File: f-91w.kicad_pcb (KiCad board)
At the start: 4 copper layers, 24.4 x 24.4 mm, 93 parts, among them P1 CONN_01X01, P10 CONN_01X01, P11 CONN_01X01, P13 CONN_01X01, P14 CONN_01X01, P2 CONN_01X01, P3 CONN_01X01, P5 CONN_01X01, P6 CONN_01X01, P7 CONN_01X01, P8 CONN_01X01, P9 CONN_01X01, Q1 BC846, U1 CY8C4248LQI-BL483, U2 LCD-F-91W, U3 BME680, Y1 32.768KHz, Y2 24MHz

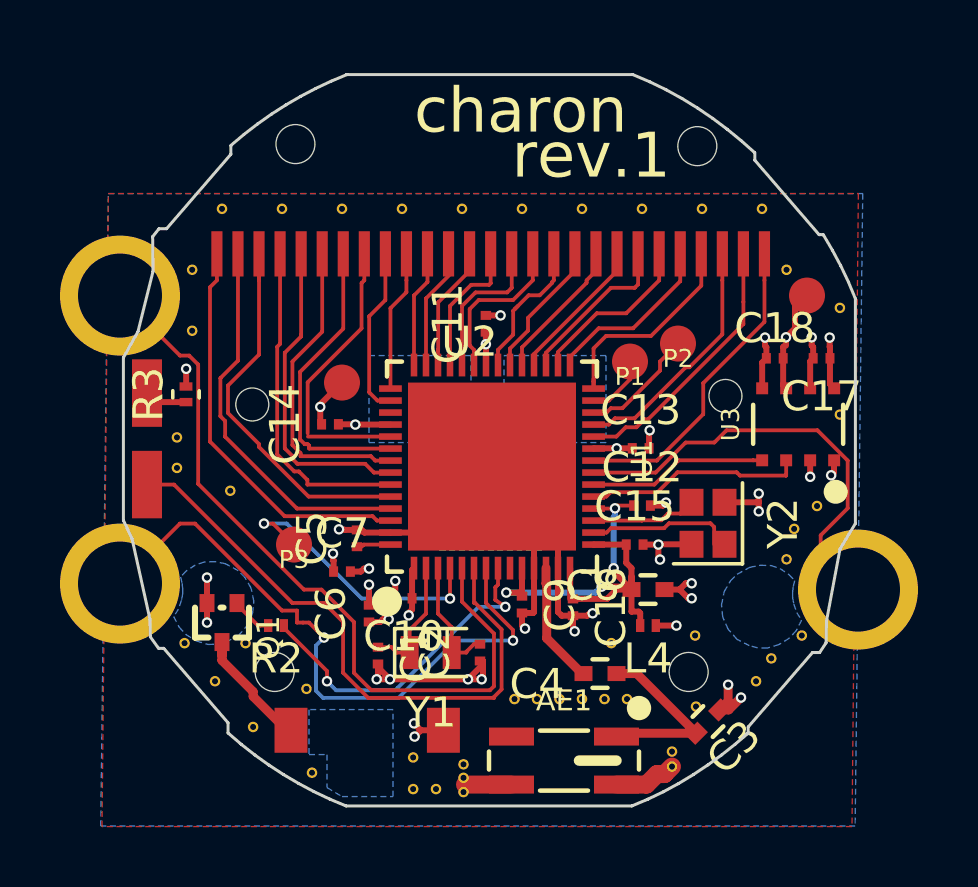
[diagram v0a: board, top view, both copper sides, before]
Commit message: Tidy silkscreen and gloss some tracks for demo
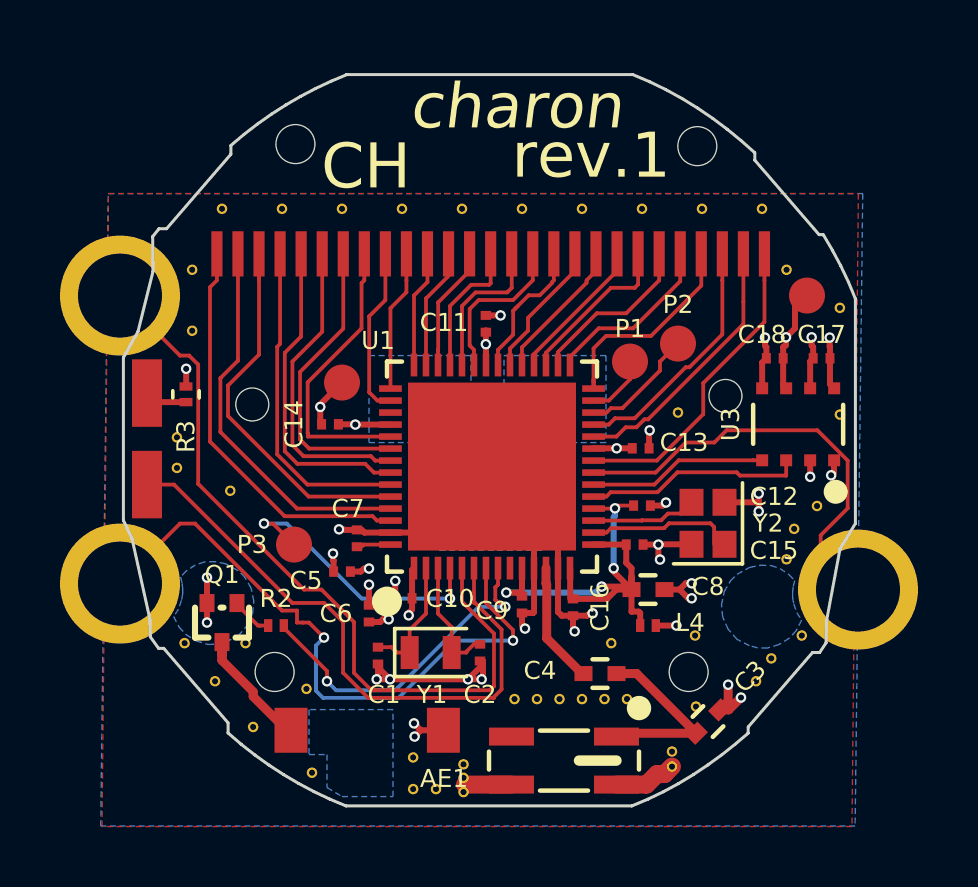
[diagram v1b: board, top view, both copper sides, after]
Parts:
- added REF**: STITCHING_VIA_0.2mm, f-91w:STITCHING_VIA_0.2mm, F.Cu at (64.2, 96.2)
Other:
- board text added: "CH"

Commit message: Make antenna trace 50R coplanar to match eurocircuits stackup
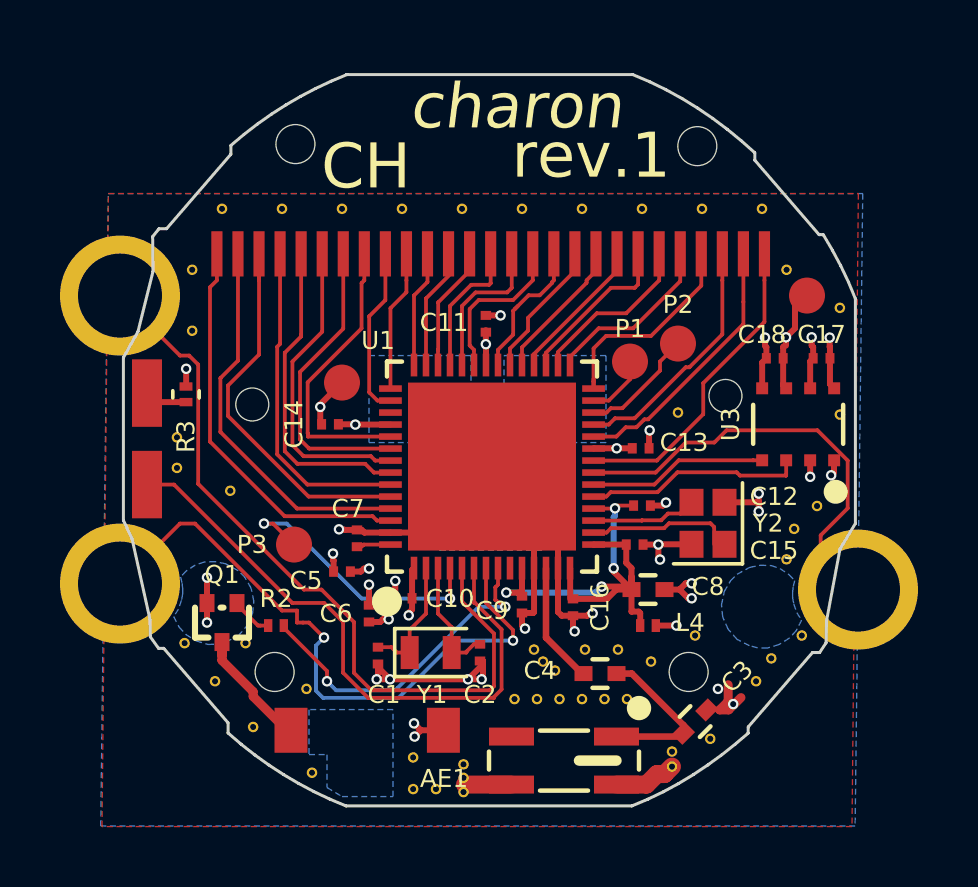
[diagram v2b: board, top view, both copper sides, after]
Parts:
- removed the REF** at (64.8, 106.0)
- added REF**: STITCHING_VIA_0.2mm, f-91w:STITCHING_VIA_0.2mm, F.Cu at (65.3, 107.1)
- added REF**: STITCHING_VIA_0.2mm, f-91w:STITCHING_VIA_0.2mm, F.Cu at (59.7, 104.5)
- added REF**: STITCHING_VIA_0.2mm, f-91w:STITCHING_VIA_0.2mm, F.Cu at (63.3, 104.5)
- added REF**: STITCHING_VIA_0.2mm, f-91w:STITCHING_VIA_0.2mm, F.Cu at (61.1, 104.1)
- added REF**: STITCHING_VIA_0.2mm, f-91w:STITCHING_VIA_0.2mm, F.Cu at (59.4, 104.1)
- added REF**: STITCHING_VIA_0.2mm, f-91w:STITCHING_VIA_0.2mm, F.Cu at (60.1, 104.8)
- moved C3 0.43 mm to (64.8, 106.5)
- moved REF** 0.31 mm to (62.2, 104.1)
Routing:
- net Net-(AE1-Pad1): track 6.19 -> 5.49 mm
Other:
- net class ANT added: clearance 0.18, trace_width 0.22, via_dia 0.35, via_drill 0.2
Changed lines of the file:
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@@
     (links 153)
     (no_connects 0)
-    (area 45.663181 84.883147 70.163247 109.362848)
+    (area 39.501571 84.8 74.608715 110.532)
     (thickness 0.6)
     (drawings 509)
-    (tracks 518)
+    (tracks 517)
     (zones 0)
-    (modules 94)
+    (modules 99)
     (nets 51)
   )
@@
   (layers
     (0 F.Cu signal)
-    (1 In1.Cu power hide)
-    (2 In2.Cu signal hide)
+    (1 In1.Cu power)
+    (2 In2.Cu signal)
     (31 B.Cu signal)
     (32 B.Adhes user hide)
@@
     (39 F.Mask user)
     (40 Dwgs.User user hide)
-    (41 Cmts.User user)
+    (41 Cmts.User user hide)
     (42 Eco1.User user hide)
     (43 Eco2.User user hide)
@@
     (visible_elements 7FFEFF7F)
     (pcbplotparams
-      (layerselection 0x010f0_80000001)
+      (layerselection 0x010f0_80000007)
       (usegerberextensions true)
       (excludeedgelayer true)
@@
     (add_net /SWCLK)
     (add_net /SWDIO)
-    (add_net "Net-(AE1-Pad1)")
     (add_net "Net-(C1-Pad1)")
     (add_net "Net-(C2-Pad1)")
-    (add_net "Net-(C4-Pad1)")
     (add_net "Net-(C5-Pad2)")
     (add_net "Net-(P10-Pad1)")
@@
     (add_net "Net-(U1-Pad16)")
     (add_net "Net-(U1-Pad17)")
+  )
+  (net_class ANT ""
+    (clearance 0.18)
+    (trace_width 0.22)
+    (via_dia 0.35)
+    (via_drill 0.2)
+    (uvia_dia 0.3)
+    (uvia_drill 0.1)
+    (add_net "Net-(AE1-Pad1)")
+    (add_net "Net-(C4-Pad1)")
   )
   (net_class PWR ""
@@
   )
   (module f-91w:STITCHING_VIA_0.2mm (layer F.Cu)
+    (at 65.275 107.075)
+    (fp_text reference REF** (at 0 1) (layer F.SilkS) hide
+      (effects (font (size 0.6 0.6) (thickness 0.15)))
+    )
+    (fp_text value STITCHING_VIA_0.2mm (at 0 -0.5) (layer F.Fab) hide
+      (effects (font (size 0.6 0.6) (thickness 0.15)))
+    )
+    (pad 1 thru_hole circle (at 0 0) (size 0.35 0.35) (drill 0.2) (layers *.Cu)
+      (net 2 GND) (zone_connect 2))
+  )
+  (module f-91w:STITCHING_VIA_0.2mm (layer F.Cu)
+    (at 59.7 104.5)
+    (fp_text reference REF** (at 0 1) (layer F.SilkS) hide
+      (effects (font (size 0.6 0.6) (thickness 0.15)))
+    )
+    (fp_text value STITCHING_VIA_0.2mm (at 0 -0.5) (layer F.Fab) hide
+      (effects (font (size 0.6 0.6) (thickness 0.15)))
+    )
+    (pad 1 thru_hole circle (at 0 0) (size 0.35 0.35) (drill 0.2) (layers *.Cu)
+      (net 2 GND) (zone_connect 2))
+  )
+  (module f-91w:STITCHING_VIA_0.2mm (layer F.Cu)
+    (at 63.3 104.5)
+    (fp_text reference REF** (at 0 1) (layer F.SilkS) hide
+      (effects (font (size 0.6 0.6) (thickness 0.15)))
+    )
+    (fp_text value STITCHING_VIA_0.2mm (at 0 -0.5) (layer F.Fab) hide
+      (effects (font (size 0.6 0.6) (thickness 0.15)))
+    )
+    (pad 1 thru_hole circle (at 0 0) (size 0.35 0.35) (drill 0.2) (layers *.Cu)
+      (net 2 GND) (zone_connect 2))
+  )
+  (module f-91w:STITCHING_VIA_0.2mm (layer F.Cu)
+    (at 61.1 104.1)
+    (fp_text reference REF** (at 0 1) (layer F.SilkS) hide
+      (effects (font (size 0.6 0.6) (thickness 0.15)))
+    )
+    (fp_text value STITCHING_VIA_0.2mm (at 0 -0.5) (layer F.Fab) hide
+      (effects (font (size 0.6 0.6) (thickness 0.15)))
+    )
+    (pad 1 thru_hole circle (at 0 0) (size 0.35 0.35) (drill 0.2) (layers *.Cu)
+      (net 2 GND) (zone_connect 2))
+  )
+  (module f-91w:STITCHING_VIA_0.2mm (layer F.Cu)
+    (at 59.4 104.1)
+    (fp_text reference REF** (at 0 1) (layer F.SilkS) hide
+      (effects (font (size 0.6 0.6) (thickness 0.15)))
+    )
+    (fp_text value STITCHING_VIA_0.2mm (at 0 -0.5) (layer F.Fab) hide
+      (effects (font (size 0.6 0.6) (thickness 0.15)))
+    )
+    (pad 1 thru_hole circle (at 0 0) (size 0.35 0.35) (drill 0.2) (layers *.Cu)
+      (net 2 GND) (zone_connect 2))
+  )
+  (module f-91w:STITCHING_VIA_0.2mm (layer F.Cu)
+    (at 60.1 104.8)
+    (fp_text reference REF** (at 0 1) (layer F.SilkS) hide
+      (effects (font (size 0.6 0.6) (thickness 0.15)))
+    )
+    (fp_text value STITCHING_VIA_0.2mm (at 0 -0.5) (layer F.Fab) hide
+      (effects (font (size 0.6 0.6) (thickness 0.15)))
+    )
+    (pad 1 thru_hole circle (at 0 0) (size 0.35 0.35) (drill 0.2) (layers *.Cu)
+      (net 2 GND) (zone_connect 2))
+  )
+  (module f-91w:STITCHING_VIA_0.2mm (layer F.Cu)
     (at 64.2 96.2)
     (fp_text reference REF** (at 0 1) (layer F.SilkS) hide
@@
   )
   (module f-91w:STITCHING_VIA_0.2mm (layer F.Cu)
-    (at 64.8 106)
-    (fp_text reference REF** (at 0 1) (layer F.SilkS) hide
-      (effects (font (size 0.6 0.6) (thickness 0.15)))
-    )
-    (fp_text value STITCHING_VIA_0.2mm (at 0 -0.5) (layer F.Fab) hide
-      (effects (font (size 0.6 0.6) (thickness 0.15)))
-    )
-    (pad 1 thru_hole circle (at 0 0) (size 0.35 0.35) (drill 0.2) (layers *.Cu)
-      (net 2 GND) (zone_connect 2))
-  )
-  (module f-91w:STITCHING_VIA_0.2mm (layer F.Cu)
     (at 62.5 105.75)
     (fp_text reference REF** (at 0 1) (layer F.SilkS) hide
@@
   )
   (module f-91w:STITCHING_VIA_0.2mm (layer F.Cu)
-    (at 61.976 103.886)
+    (at 62.2 104.1)
     (fp_text reference REF** (at 0 1) (layer F.SilkS) hide
       (effects (font (size 0.6 0.6) (thickness 0.15)))
@@
   )
   (module Capacitors_SMD:C_0402 (layer F.Cu)
-    (at 65.2 106.5 45)
+    (at 64.77 106.5 45)
     (descr "Capacitor SMD 0402, reflow soldering, AVX (see smccp.pdf)")
     (tags "capacitor 0402")
@@
   (segment (start 65.588909 106.111091) (end 65.888909 106.111091) (width 0.3) (layer F.Cu) (net 2))
   (segment (start 65.888909 106.111091) (end 66.3 105.7) (width 0.3) (layer F.Cu) (net 2))
-  (via (at 66.3 105.7) (size 0.35) (drill 0.2) (layers F.Cu B.Cu) (net 2))
-  (via (at 65.871751 105.271751) (size 0.35) (drill 0.2) (layers F.Cu B.Cu) (net 2))
+  (via (at 66.04 105.918) (size 0.35) (drill 0.2) (layers F.Cu B.Cu) (net 2))
+  (via (at 65.532 105.41) (size 0.35) (drill 0.2) (layers F.Cu B.Cu) (net 2))
   (segment (start 65.588909 106.111091) (end 65.871751 105.828249) (width 0.3) (layer F.Cu) (net 2))
   (segment (start 65.871751 105.828249) (end 65.871751 105.271751) (width 0.3) (layer F.Cu) (net 2))
@@
   (segment (start 56.2 101.385) (end 56.2 102.9) (width 0.127) (layer F.Cu) (net 40))
   (segment (start 56.2 102.9) (end 56.6555 103.3555) (width 0.127) (layer F.Cu) (net 40))
-  (segment (start 64.811091 106.888909) (end 62.261091 106.888909) (width 0.3) (layer F.Cu) (net 41))
-  (segment (start 62.261091 106.888909) (end 62.15 107) (width 0.3) (layer F.Cu) (net 41))
-  (segment (start 62.15 104.9) (end 62.822182 104.9) (width 0.3) (layer F.Cu) (net 41))
-  (segment (start 62.822182 104.9) (end 64.811091 106.888909) (width 0.3) (layer F.Cu) (net 41))
-  (segment (start 59.8 101.385) (end 59.8 101.9) (width 0.3) (layer F.Cu) (net 42))
-  (segment (start 59.8 101.9) (end 59.82299 101.92299) (width 0.3) (layer F.Cu) (net 42))
-  (segment (start 59.82299 101.92299) (end 59.82299 103.72299) (width 0.3) (layer F.Cu) (net 42))
-  (segment (start 59.82299 103.72299) (end 61 104.9) (width 0.3) (layer F.Cu) (net 42))
-  (segment (start 61 104.9) (end 61.05 104.9) (width 0.3) (layer F.Cu) (net 42))
+  (segment (start 62.15 107) (end 64.27 107) (width 0.22) (layer F.Cu) (net 41))
+  (segment (start 64.27 107) (end 64.381091 106.888909) (width 0.21) (layer F.Cu) (net 41))
+  (segment (start 62.15 104.9) (end 62.66 104.9) (width 0.22) (layer F.Cu) (net 41))
+  (segment (start 62.66 104.9) (end 64.381091 106.621091) (width 0.22) (layer F.Cu) (net 41))
+  (segment (start 64.381091 106.621091) (end 64.381091 106.888909) (width 0.22) (layer F.Cu) (net 41))
+  (segment (start 59.8 101.385) (end 59.8 103.7) (width 0.22) (layer F.Cu) (net 42))
+  (segment (start 59.8 103.7) (end 61 104.9) (width 0.22) (layer F.Cu) (net 42))
+  (segment (start 61 104.9) (end 61.05 104.9) (width 0.21) (layer F.Cu) (net 42))
   (segment (start 54.615 100.6) (end 53.7265 100.6) (width 0.127) (layer F.Cu) (net 43))
   (segment (start 53.7265 100.6) (end 53.6555 100.671) (width 0.127) (layer F.Cu) (net 43))

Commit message: Fix battery connection on bottom layer and DRC errors
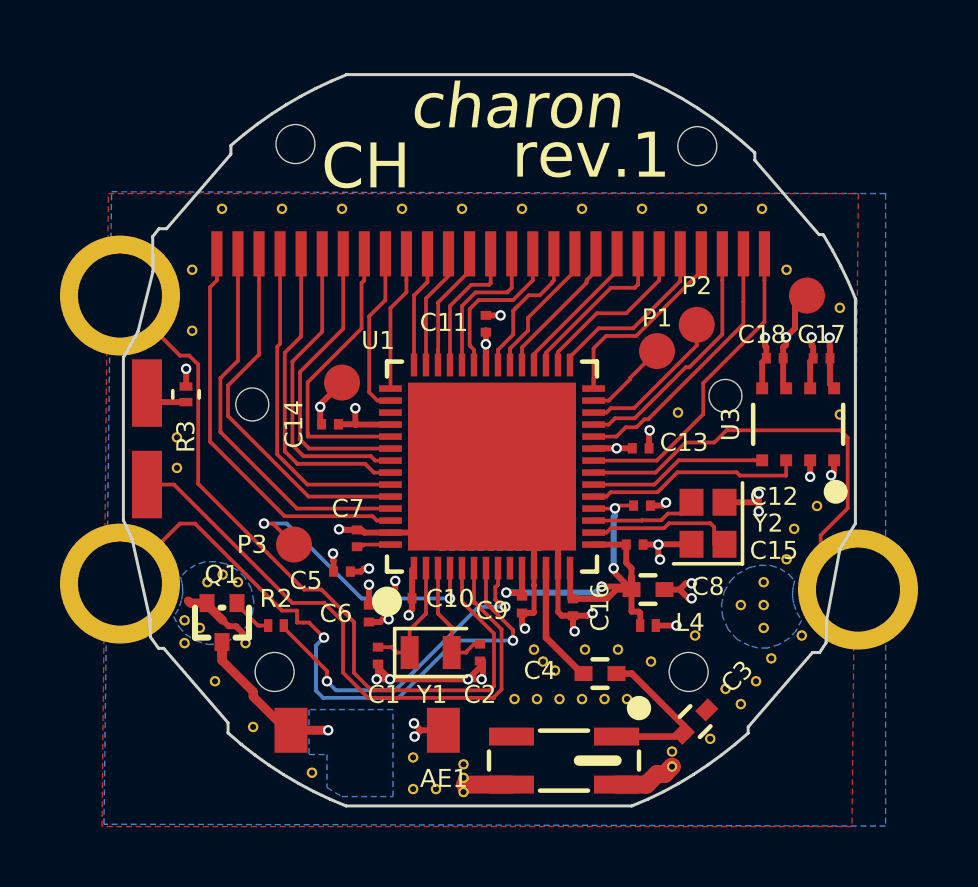
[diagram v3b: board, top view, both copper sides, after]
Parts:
- removed the REF** at (51.8, 105.4)
- removed the REF** at (49.3, 98.8)
- added REF**: STITCHING_VIA_0.2mm, f-91w:STITCHING_VIA_0.2mm, F.Cu at (65.8, 105.4)
- added REF**: STITCHING_VIA_0.2mm, f-91w:STITCHING_VIA_0.2mm, F.Cu at (67.1, 101.9)
- added REF**: STITCHING_VIA_0.2mm, f-91w:STITCHING_VIA_0.2mm, F.Cu at (66.3, 105.9)
- added REF**: STITCHING_VIA_0.2mm, f-91w:STITCHING_VIA_0.2mm, F.Cu at (48.3, 103.4)
- added REF**: STITCHING_VIA_0.2mm, f-91w:STITCHING_VIA_0.2mm, F.Cu at (49.0, 101.6)
- added REF**: STITCHING_VIA_0.2mm, f-91w:STITCHING_VIA_0.2mm, F.Cu at (49.5, 101.9)
- added REF**: STITCHING_VIA_0.2mm, f-91w:STITCHING_VIA_0.2mm, F.Cu at (47.8, 103.1)
- added REF**: STITCHING_VIA_0.2mm, f-91w:STITCHING_VIA_0.2mm, F.Cu at (67.1, 102.6)
- added REF**: STITCHING_VIA_0.2mm, f-91w:STITCHING_VIA_0.2mm, F.Cu at (48.5, 101.9)
- added REF**: STITCHING_VIA_0.2mm, f-91w:STITCHING_VIA_0.2mm, F.Cu at (67.1, 103.4)
- added REF**: STITCHING_VIA_0.2mm, f-91w:STITCHING_VIA_0.2mm, F.Cu at (66.3, 102.6)
- moved P1 0.97 mm to (63.5, 94.2)
- moved P2 0.88 mm to (64.8, 93.3)
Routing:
- net /BUZ: track 4.53 -> 5.77 mm, vias 0 -> 1
- net /SWDIO: track 3.94 -> 5.05 mm
- net /LCD_SEG21: track 7.76 -> 6.90 mm
- net /SWCLK: track 2.00 -> 2.82 mm
- net VCC: track 15.8 -> 16.6 mm
- net GND: track 47.6 -> 47.0 mm, vias 28 -> 24

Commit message: Add ground vias in QFN centre pad
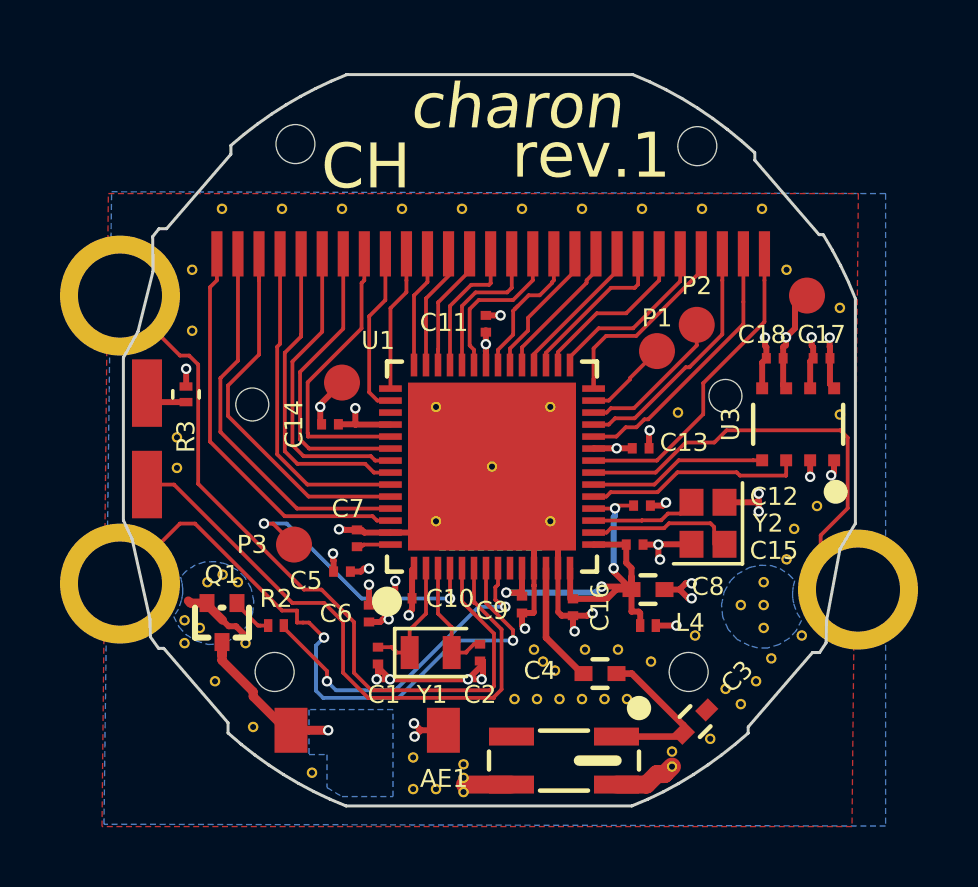
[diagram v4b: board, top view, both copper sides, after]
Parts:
- added REF**: STITCHING_VIA_0.2mm, f-91w:STITCHING_VIA_0.2mm, F.Cu at (58.0, 98.0)
- added REF**: STITCHING_VIA_0.2mm, f-91w:STITCHING_VIA_0.2mm, F.Cu at (59.9, 99.8)
- added REF**: STITCHING_VIA_0.2mm, f-91w:STITCHING_VIA_0.2mm, F.Cu at (56.1, 99.8)
- added REF**: STITCHING_VIA_0.2mm, f-91w:STITCHING_VIA_0.2mm, F.Cu at (56.1, 96.0)
- added REF**: STITCHING_VIA_0.2mm, f-91w:STITCHING_VIA_0.2mm, F.Cu at (59.9, 96.0)
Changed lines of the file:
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@@
     (tracks 518)
     (zones 0)
-    (modules 108)
+    (modules 113)
     (nets 51)
   )
@@
     (35 F.Paste user hide)
     (36 B.SilkS user hide)
-    (37 F.SilkS user hide)
+    (37 F.SilkS user)
     (38 B.Mask user)
     (39 F.Mask user hide)
@@
   )
   (module f-91w:STITCHING_VIA_0.2mm (layer F.Cu)
+    (at 58 98)
+    (fp_text reference REF** (at 0 1) (layer F.SilkS) hide
+      (effects (font (size 0.6 0.6) (thickness 0.15)))
+    )
+    (fp_text value STITCHING_VIA_0.2mm (at 0 -0.5) (layer F.Fab) hide
+      (effects (font (size 0.6 0.6) (thickness 0.15)))
+    )
+    (pad 1 thru_hole circle (at 0 0) (size 0.35 0.35) (drill 0.2) (layers *.Cu)
+      (net 2 GND) (zone_connect 2))
+  )
+  (module f-91w:STITCHING_VIA_0.2mm (layer F.Cu)
+    (at 59.944 99.822)
+    (fp_text reference REF** (at 0 1) (layer F.SilkS) hide
+      (effects (font (size 0.6 0.6) (thickness 0.15)))
+    )
+    (fp_text value STITCHING_VIA_0.2mm (at 0 -0.5) (layer F.Fab) hide
+      (effects (font (size 0.6 0.6) (thickness 0.15)))
+    )
+    (pad 1 thru_hole circle (at 0 0) (size 0.35 0.35) (drill 0.2) (layers *.Cu)
+      (net 2 GND) (zone_connect 2))
+  )
+  (module f-91w:STITCHING_VIA_0.2mm (layer F.Cu)
+    (at 56.134 99.822)
+    (fp_text reference REF** (at 0 1) (layer F.SilkS) hide
+      (effects (font (size 0.6 0.6) (thickness 0.15)))
+    )
+    (fp_text value STITCHING_VIA_0.2mm (at 0 -0.5) (layer F.Fab) hide
+      (effects (font (size 0.6 0.6) (thickness 0.15)))
+    )
+    (pad 1 thru_hole circle (at 0 0) (size 0.35 0.35) (drill 0.2) (layers *.Cu)
+      (net 2 GND) (zone_connect 2))
+  )
+  (module f-91w:STITCHING_VIA_0.2mm (layer F.Cu)
+    (at 56.134 96.012)
+    (fp_text reference REF** (at 0 1) (layer F.SilkS) hide
+      (effects (font (size 0.6 0.6) (thickness 0.15)))
+    )
+    (fp_text value STITCHING_VIA_0.2mm (at 0 -0.5) (layer F.Fab) hide
+      (effects (font (size 0.6 0.6) (thickness 0.15)))
+    )
+    (pad 1 thru_hole circle (at 0 0) (size 0.35 0.35) (drill 0.2) (layers *.Cu)
+      (net 2 GND) (zone_connect 2))
+  )
+  (module f-91w:STITCHING_VIA_0.2mm (layer F.Cu)
+    (at 59.944 96.012)
+    (fp_text reference REF** (at 0 1) (layer F.SilkS) hide
+      (effects (font (size 0.6 0.6) (thickness 0.15)))
+    )
+    (fp_text value STITCHING_VIA_0.2mm (at 0 -0.5) (layer F.Fab) hide
+      (effects (font (size 0.6 0.6) (thickness 0.15)))
+    )
+    (pad 1 thru_hole circle (at 0 0) (size 0.35 0.35) (drill 0.2) (layers *.Cu)
+      (net 2 GND) (zone_connect 2))
+  )
+  (module f-91w:STITCHING_VIA_0.2mm (layer F.Cu)
